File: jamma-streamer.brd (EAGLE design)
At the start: 180.3 x 92 mm, 64 parts, among them IC1 LM7805, J1 Audio line out, J2 ICSP, J4 DM3AT-SF-PEJM5, J5 KMMX-BSMT35S-B30TR, T1 TY-145P, T2 TY-145P, U1 CD74HC165MD16-M, U10 LM358DTD8-M, U2 ATMEGA328PB-AUR, U3 74HC4050D, U4 TLV757X / LP298X, U5 CD74HC165MD16-M, U6 CD74HC165MD16-M, U7 FT232RL, U8 DS3231SNT&R21-0042B_16-M, U9 NDT2955SOT-223-M, Y1 16MHz

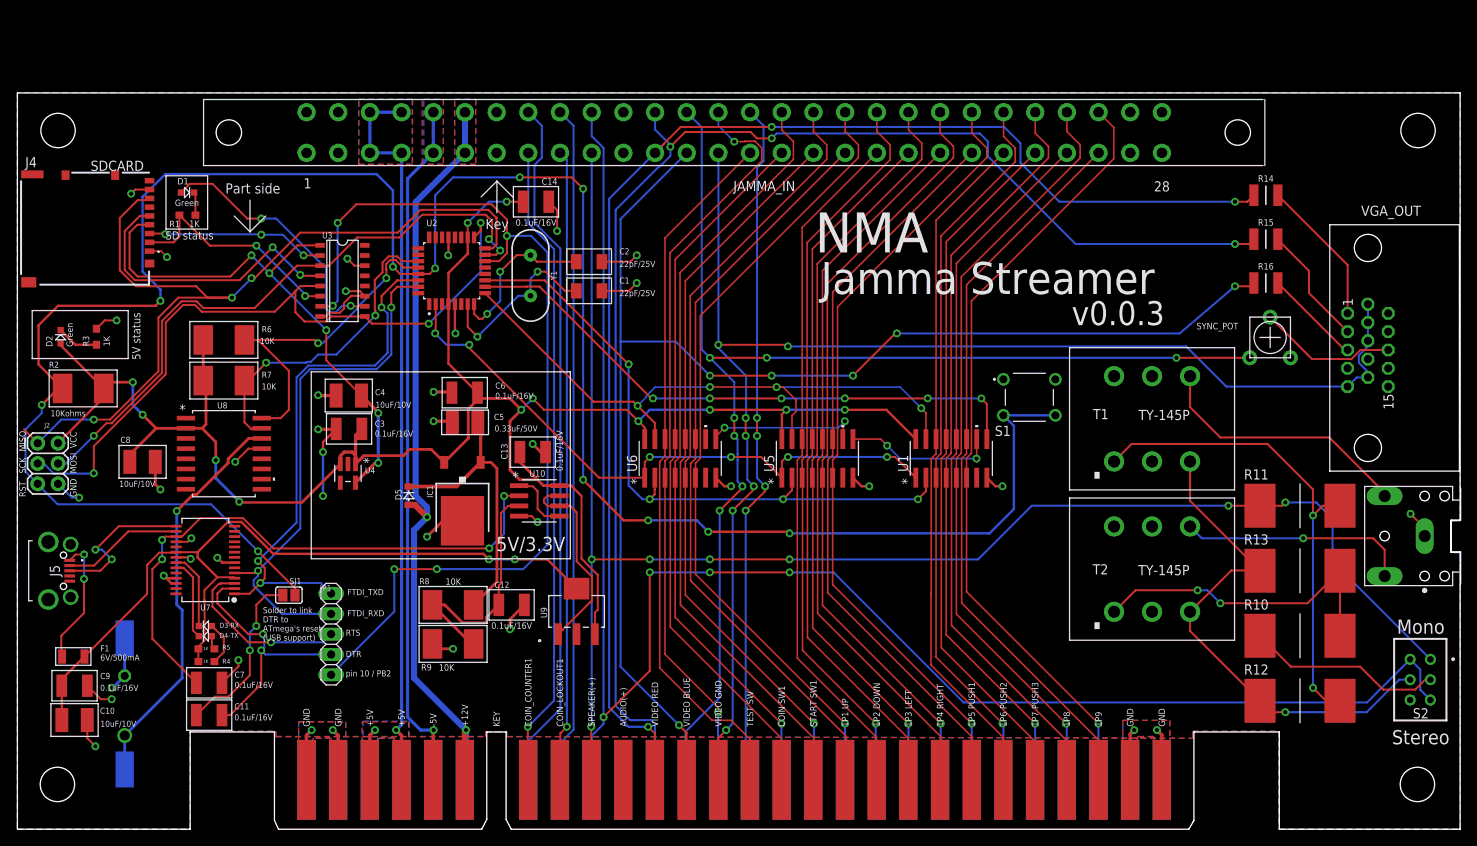
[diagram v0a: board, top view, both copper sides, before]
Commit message: Reorg eagle libraries
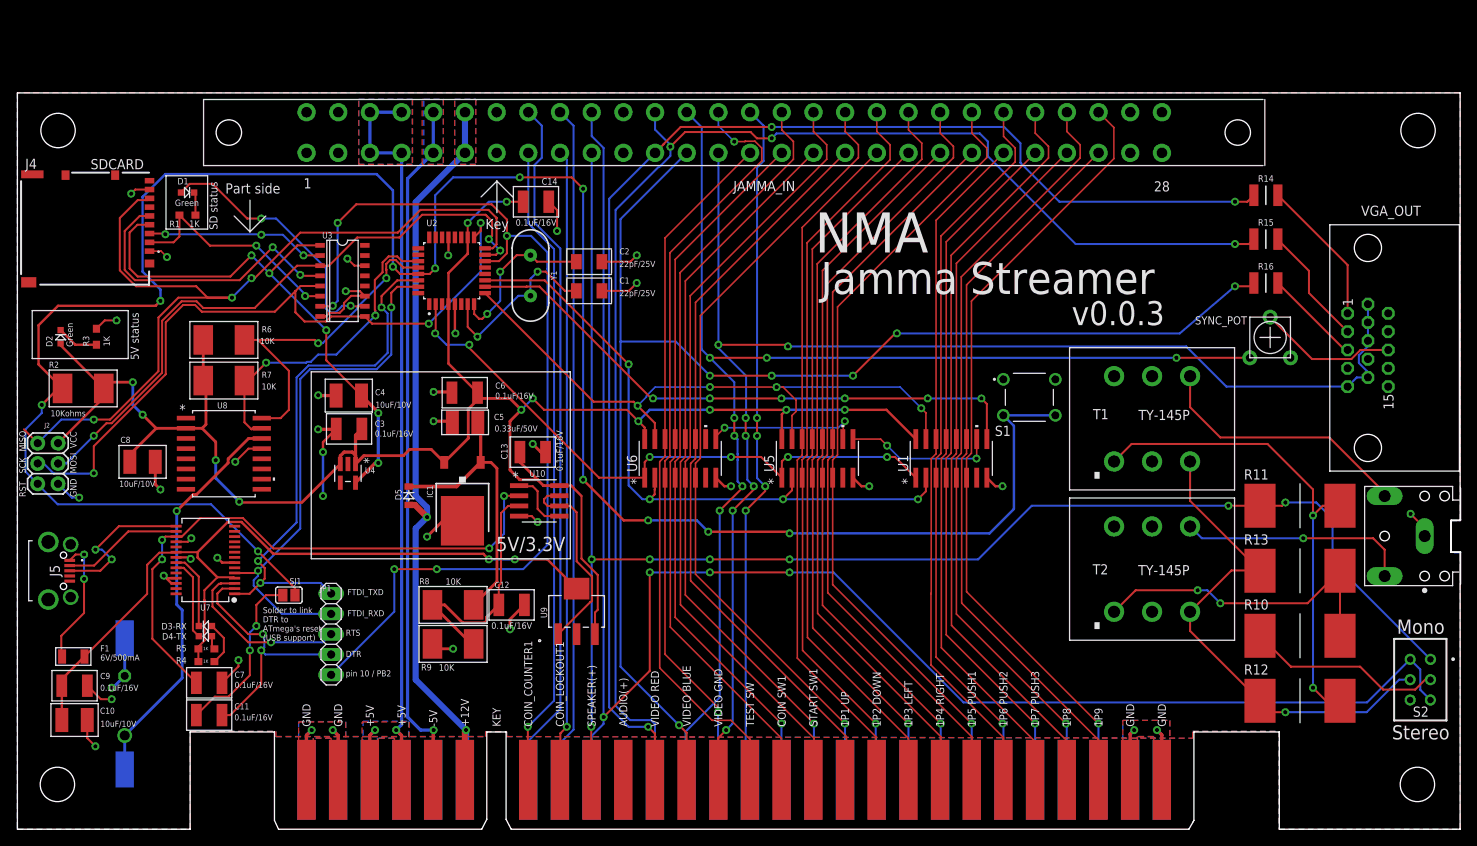
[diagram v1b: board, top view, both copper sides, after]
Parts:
- B1: device S8411R:S8411-45R -> nma-eagle:S8411-45R
- C1, C2: device CMS:KEMET-C1206C334M5RAC -> nma-eagle:KEMET-C1206C334M5RAC
- C10, C4, C8: device CMS:KEMET-C1210C106K8N -> nma-eagle:KEMET-C1210C106K8N
- C11, C12, C13, C14, C3, C6, C7, C9: device CMS:KEMET-C1210C104K4J -> nma-eagle:KEMET-C1210C104K4J
- C5: device CMS:KEMET-C1206X334K5R -> nma-eagle:KEMET-C1206X334K5R
- D1, D2, D3-RX, D4-TX: device CMS:604-APTD1608LCGCK -> nma-eagle:604-APTD1608LCGCK
- D5: device RRE07VTM4SFHTR:DIODE-RRE07VTM4SFHTR -> nma-eagle:DIODE-RRE07VTM4SFHTR
- F1: device 1206L050YR:FUSE-1206L050YR -> nma-eagle:FUSE-1206L050YR
- J1: device SJ1-3523N:CUI_SJ1-3523N -> nma-eagle:CUI_SJ1-3523N
- J4: device DM3AT-SF-PEJM5:DM3AT-SF-PEJM5_1 -> nma-eagle:DM3AT-SF-PEJM5_1
- J5: device KMMX-BSMT35S-B30TR:KMMXBSMT35SB30TR -> nma-eagle:KMMXBSMT35SB30TR
- JAMMA_IN: device jamma_female_56:JAMMA_FEMALE_56 -> nma-eagle:JAMMA_FEMALE_56
- JAMMA_OUT_BTM: device JAMMA:JAMMA_BOTTOM -> nma-eagle:JAMMA_BOTTOM
- JAMMA_OUT_TOP: device JAMMA:JAMMA_TOP -> nma-eagle:JAMMA_TOP
- R1, R3, R4, R5: device CMS:652-CHP0603FX1001ELF -> nma-eagle:652-CHP0603FX1001ELF
- R10, R11, R12, R13: device nma-mouser:TE_3550_SERIES -> nma-eagle:TE_3550_SERIES
- R14, R15, R16: device nma-mouser:RESC3225X70N -> nma-eagle:RESC3225X70N
- R2, R6, R7, R8, R9: device CMS:BOURNS-CRM2512AJW-103ELF -> nma-eagle:BOURNS-CRM2512AJW-103ELF
- S1: device 1825910-7:SW_1825910-7 -> nma-eagle:SW_1825910-7
- S2: device SamacSys_Parts:SS22SDP2(DPDT) -> nma-eagle:SS22SDP2(DPDT)
- SYNC_POT: device SparkFun-Retired:TRIM_POT_PTH -> nma-eagle:TRIM_POT_PTH
- T1, T2: device TRIAD-TY-145P:TRIAD-TY-145P -> nma-eagle:TRIAD-TY-145P
- U1, U5, U6: device CD74HC165M:D16-M -> nma-eagle:D16-M
- U10: device LM358D:D8-M -> nma-eagle:D8-M
- U2: device ATMEGA328PB-AUR:QFP80P900X900X120-32N -> nma-eagle:QFP80P900X900X120-32N
- U3: device 74HC4050D:SO16 -> nma-eagle:SO16
- U4: device LP2981-33DBVR:DBV5-M -> nma-eagle:DBV5-M
- U8: device DS3231:21-0042B_16-M -> nma-eagle:21-0042B_16-M
- U9: device NDT2955:SOT-223-M -> nma-eagle:SOT-223-M
- VGA_OUT: device harting-D-Sub-15:HARTING-DSUB-15-FEMALE -> nma-eagle:HARTING-DSUB-15-FEMALE
- Y1: device SparkFun-Clocks:HC49US -> nma-eagle:HC49US

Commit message: Changing battery holder to use CR2032
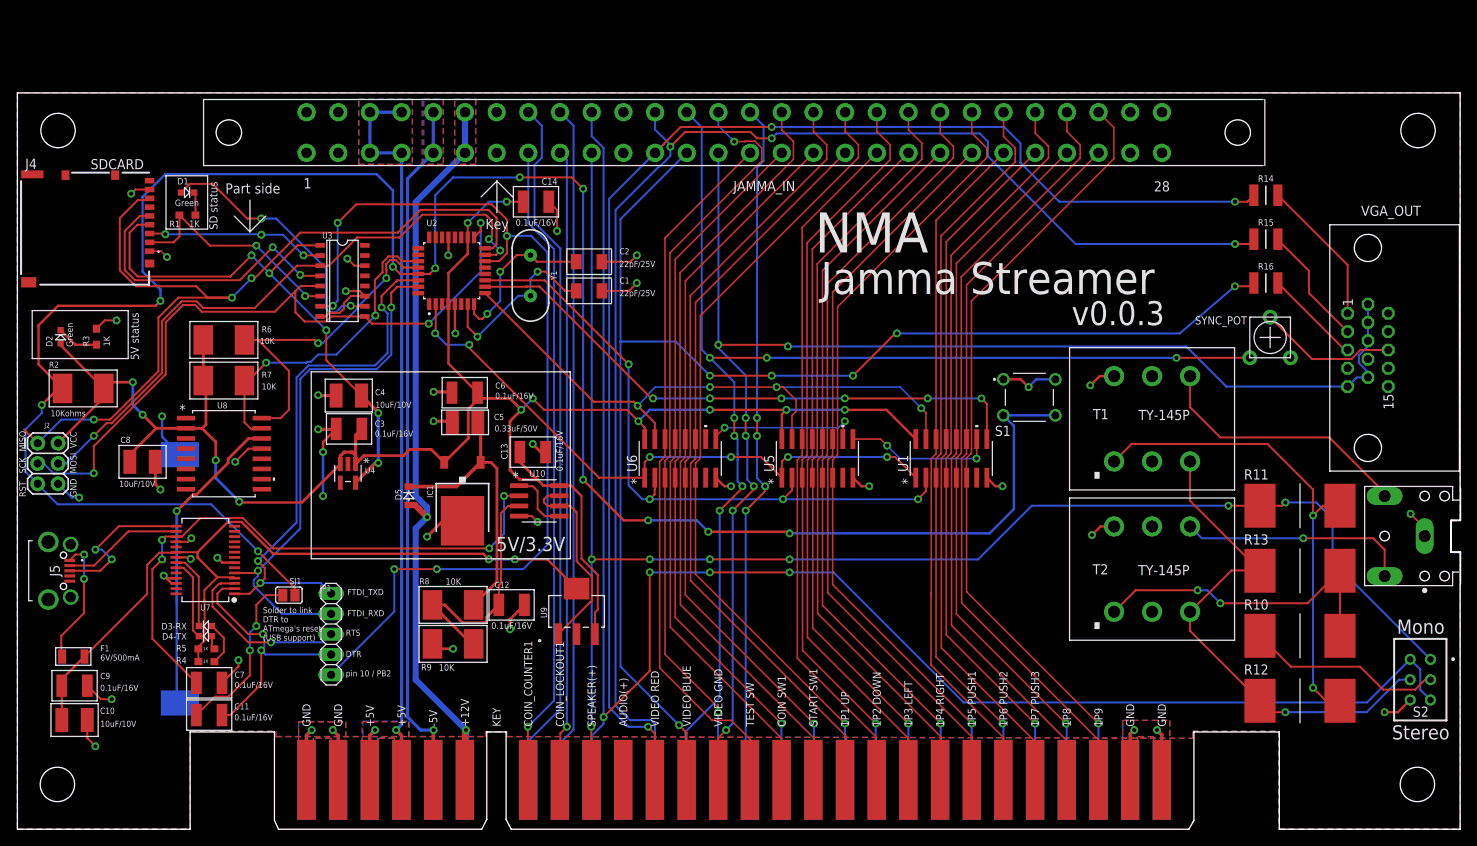
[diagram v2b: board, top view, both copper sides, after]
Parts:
- removed B1: S8411-45R, nma-eagle:S8411-45R
- added J3: 796136-1, nma-eagle:796136-1
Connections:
- net GND: now also J3.2; no longer B1.3, B1.4
- net N$31: now also J3.1; no longer B1.1, B1.2
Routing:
- net GND: track 176.3 -> 192.9 mm, vias 40 -> 44
- net N$31: track 50.2 -> 38.9 mm
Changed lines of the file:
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@@
 <layers>
 <layer number="1" name="Top" color="4" fill="1" visible="yes" active="yes"/>
-<layer number="2" name="Route2" color="16" fill="1" visible="no" active="yes"/>
+<layer number="2" name="Route2" color="16" fill="1" visible="yes" active="yes"/>
 <layer number="3" name="Route3" color="4" fill="3" visible="no" active="no"/>
 <layer number="4" name="Route4" color="1" fill="4" visible="no" active="no"/>
@@
 <layer number="13" name="Route13" color="4" fill="5" visible="no" active="no"/>
 <layer number="14" name="Route14" color="1" fill="6" visible="no" active="no"/>
-<layer number="15" name="Route15" color="23" fill="1" visible="no" active="yes"/>
+<layer number="15" name="Route15" color="23" fill="1" visible="yes" active="yes"/>
 <layer number="16" name="Bottom" color="1" fill="1" visible="yes" active="yes"/>
 <layer number="17" name="Pads" color="2" fill="1" visible="yes" active="yes"/>
@@
 <layer number="25" name="tNames" color="7" fill="1" visible="yes" active="yes"/>
 <layer number="26" name="bNames" color="7" fill="1" visible="yes" active="yes"/>
-<layer number="27" name="tValues" color="7" fill="1" visible="yes" active="yes"/>
+<layer number="27" name="tValues" color="7" fill="1" visible="no" active="yes"/>
 <layer number="28" name="bValues" color="7" fill="1" visible="no" active="yes"/>
 <layer number="29" name="tStop" color="7" fill="3" visible="no" active="yes"/>
@@
 <layer number="44" name="Drills" color="7" fill="1" visible="no" active="yes"/>
 <layer number="45" name="Holes" color="7" fill="1" visible="no" active="yes"/>
-<layer number="46" name="Milling" color="3" fill="1" visible="yes" active="yes"/>
+<layer number="46" name="Milling" color="3" fill="1" visible="no" active="yes"/>
 <layer number="47" name="Measures" color="7" fill="1" visible="no" active="yes"/>
 <layer number="48" name="Document" color="7" fill="1" visible="no" active="yes"/>
@@
 <attribute name="VALUE" x="30.5308" y="54.9656" size="0.762" layer="21"/>
 </element>
-<element name="B1" library="nma-eagle" package="S8411-45R" value="S8411-45R" x="13.4112" y="15.4432" smashed="yes" rot="MR0">
-<attribute name="NAME" x="4.9442" y="16.3732" size="1.27" layer="22" rot="MR0"/>
-</element>
 <element name="C8" library="nma-eagle" package="KEMET-C1210C106K8N" value="10uF/10V" x="15.6464" y="45.9232" smashed="yes">
 <attribute name="NAME" x="12.8728" y="48.2904" size="0.762" layer="21"/>
@@
 <attribute name="NAME" x="156.0576" y="70.3652" size="0.8128" layer="25" align="center"/>
 <attribute name="VALUE" x="156.0576" y="66.1852" size="0.8128" layer="27" align="center"/>
+</element>
+<element name="J3" library="nma-eagle" package="796136-1" value="796136-1" x="20.32" y="31.2928" smashed="yes" rot="MR90">
+<attribute name="DESCRIPTION" value="Holder pcb 2 way Battery TE Connectivity Surface Mount Battery Holder for 1, Leaf Spring Contact" x="20.32" y="31.2928" size="1.778" layer="28" rot="MR90" display="off"/>
+<attribute name="HEIGHT" value="mm" x="20.32" y="31.2928" size="1.778" layer="28" rot="MR90" display="off"/>
+<attribute name="MANUFACTURER_NAME" value="TE Connectivity" x="20.32" y="31.2928" size="1.778" layer="28" rot="MR90" display="off"/>
+<attribute name="MANUFACTURER_PART_NUMBER" value="796136-1" x="20.32" y="31.2928" size="1.778" layer="28" rot="MR90" display="off"/>
+<attribute name="MOUSER_PART_NUMBER" value="571-796136-1" x="20.32" y="31.2928" size="1.778" layer="28" rot="MR90" display="off"/>
+<attribute name="MOUSER_PRICE-STOCK" value="https://www.mouser.co.uk/ProductDetail/TE-Connectivity/796136-1?qs=PfIaAWlFPdz%252BdW7QT0YDTw%3D%3D" x="20.32" y="31.2928" size="1.778" layer="28" rot="MR90" display="off"/>
+<attribute name="NAME" x="31.83636875" y="20.66383125" size="1.27" layer="26" rot="MR90" align="center"/>
+<attribute name="VALUE" x="8.97636875" y="20.66383125" size="1.27" layer="28" rot="MR90" align="center"/>
 </element>
 </elements>
@@
 <via x="37.592" y="49.9872" extent="1-16" drill="0.508"/>
 <wire x1="19.839" y1="30.73" x2="19.8858" y2="30.6832" width="0.254" layer="1"/>
-<contactref element="B1" pad="4"/>
-<contactref element="B1" pad="3"/>
 <contactref element="U8" pad="13"/>
 <wire x1="43.435" y1="70.445" x2="42.1278" y2="70.445" width="0.254" layer="1"/>
@@
 <wire x1="28.8798" y1="47.5742" x2="27.2288" y2="45.9232" width="0.254" layer="1"/>
 <via x="27.2288" y="45.9232" extent="1-16" drill="0.508"/>
-<wire x1="13.4112" y1="23.8682" x2="13.4112" y2="19.1682" width="0.3556" layer="16"/>
-<wire x1="13.4112" y1="19.1682" x2="11.9214" y2="17.6784" width="0.3556" layer="16"/>
-<wire x1="11.9214" y1="17.6784" x2="11.7856" y2="17.6784" width="0.3556" layer="16"/>
-<via x="11.7856" y="17.6784" extent="1-16" drill="0.508"/>
 <contactref element="C8" pad="2"/>
 <wire x1="17.2364" y1="45.9232" x2="17.2364" y2="43.114" width="0.3556" layer="1"/>
@@
 <wire x1="17.9578" y1="72.263" x2="18.6944" y2="71.5264" width="0.2032" layer="1"/>
 <via x="18.6944" y="71.5264" extent="1-16" drill="0.508"/>
+<contactref element="J3" pad="2"/>
+<wire x1="20.32" y1="46.8128" x2="18.0848" y2="49.048" width="0.3048" layer="16"/>
+<wire x1="18.0848" y1="49.048" x2="18.0848" y2="51.6128" width="0.3048" layer="16"/>
+<via x="18.0848" y="51.6128" extent="1-16" drill="0.508"/>
+<wire x1="174.0916" y1="16.1544" x2="172.5676" y2="14.6304" width="0.3048" layer="1"/>
+<wire x1="172.5676" y1="14.6304" x2="170.8912" y2="14.6304" width="0.3048" layer="1"/>
+<via x="170.8912" y="14.6304" extent="1-16" drill="0.508"/>
+<wire x1="137.0838" y1="37.846" x2="135.382" y2="37.846" width="0.3048" layer="1"/>
+<wire x1="135.382" y1="37.846" x2="134.3152" y2="36.7792" width="0.3048" layer="1"/>
+<via x="134.3152" y="36.7792" extent="1-16" drill="0.508"/>
+<wire x1="137.0838" y1="56.63565" x2="135.27405" y2="56.63565" width="0.3048" layer="1"/>
+<wire x1="135.27405" y1="56.63565" x2="134.112" y2="55.4736" width="0.3048" layer="1"/>
+<via x="134.112" y="55.4736" extent="1-16" drill="0.508"/>
+<wire x1="129.74335" y1="56.23855" x2="127.35855" y2="56.23855" width="0.3048" layer="16"/>
+<wire x1="127.35855" y1="56.23855" x2="126.3904" y2="55.2704" width="0.3048" layer="16"/>
+<via x="126.3904" y="55.2704" extent="1-16" drill="0.508"/>
+<wire x1="123.24335" y1="56.23855" x2="125.42225" y2="56.23855" width="0.3048" layer="1"/>
+<wire x1="125.42225" y1="56.23855" x2="126.3904" y2="55.2704" width="0.3048" layer="1"/>
 </signal>
 <signal name="VGROUND">
@@
 <signal name="N$31">
 <contactref element="U8" pad="14"/>
-<contactref element="B1" pad="1"/>
-<contactref element="B1" pad="2"/>
-<wire x1="13.4112" y1="7.4682" x2="13.4112" y2="11.7182" width="0.3556" layer="16"/>
 <via x="19.9136" y="39.7764" extent="1-16" drill="0.508"/>
-<wire x1="19.9136" y1="28.0796375" x2="19.9136" y2="30.6832" width="0.3556" layer="16"/>
-<wire x1="19.9136" y1="39.7764" x2="19.9136" y2="30.6832" width="0.3556" layer="16"/>
-<wire x1="20.5994" y1="27.3938375" x2="19.9136" y2="28.0796375" width="0.3556" layer="16"/>
-<wire x1="20.5994" y1="18.9064" x2="20.5994" y2="27.3938375" width="0.3556" layer="16"/>
-<wire x1="13.4112" y1="11.7182" x2="20.5994" y2="18.9064" width="0.3556" layer="16"/>
+<wire x1="19.9136" y1="39.7764" x2="19.9136" y2="28.0796375" width="0.3556" layer="16"/>
 <wire x1="19.9136" y1="39.7764" x2="21.9583" y2="41.8211" width="0.3556" layer="1"/>
 <wire x1="21.9583" y1="41.8211" x2="22.3701125" y2="41.8211" width="0.3556" layer="1"/>
@@
 <wire x1="26.3398" y1="46.2914375" x2="28.8925625" y2="48.8442" width="0.3556" layer="1"/>
 <wire x1="28.8925625" y1="48.8442" x2="30.5435" y2="48.8442" width="0.3556" layer="1"/>
+<contactref element="J3" pad="1"/>
+<wire x1="19.9136" y1="28.0796375" x2="19.9136" y2="16.1792" width="0.3048" layer="16"/>
+<wire x1="19.9136" y1="16.1792" x2="20.32" y2="15.7728" width="0.3048" layer="16"/>
 </signal>
 <signal name="USBVCC">

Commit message: Added RTC with milliseconds accuracy
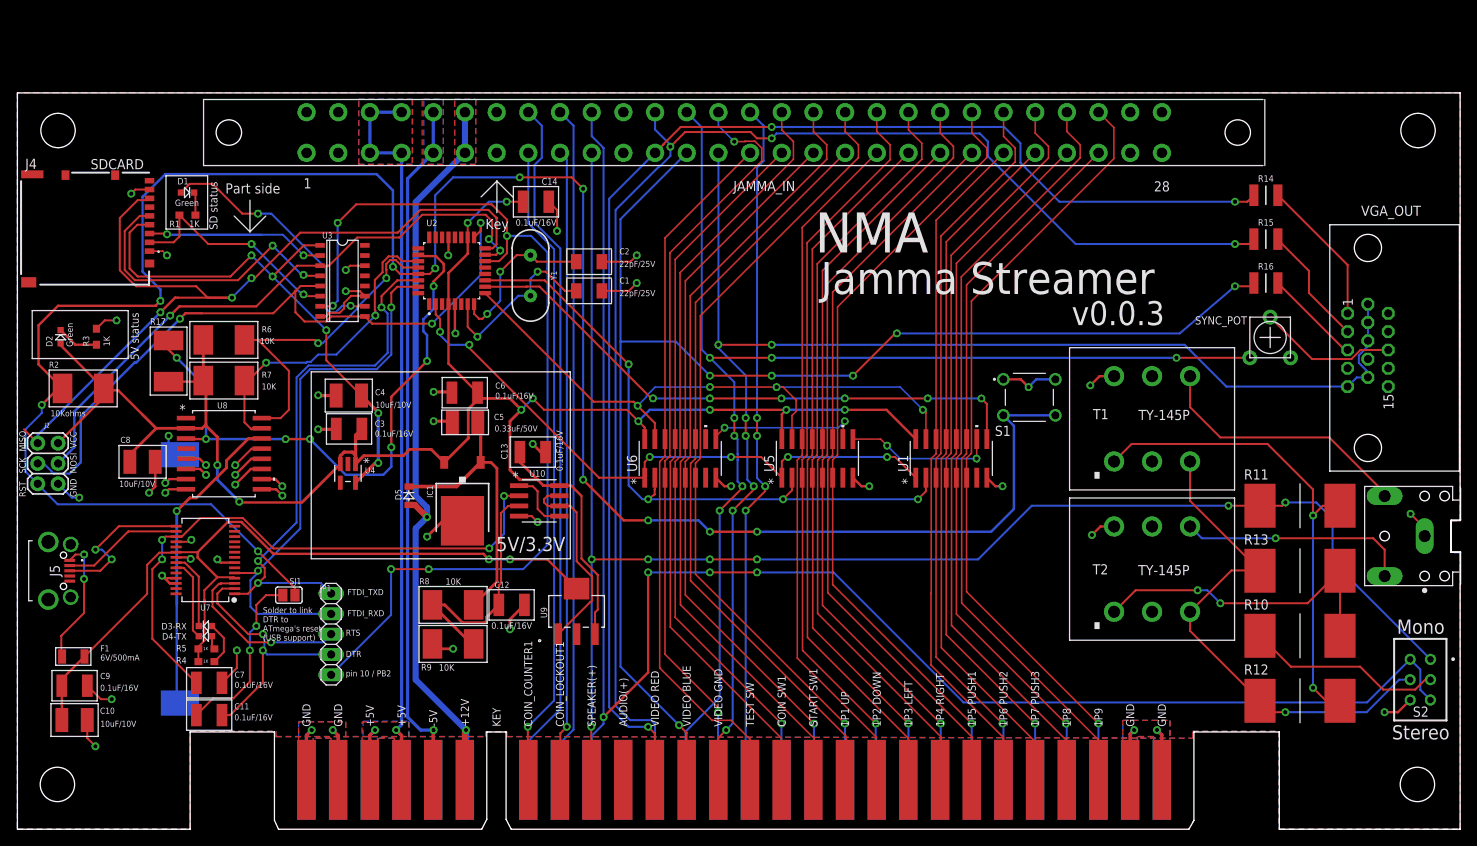
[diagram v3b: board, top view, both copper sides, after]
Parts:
- added R17: 10K, nma-eagle:BOURNS-CRM2512AJW-103ELF
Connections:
- new net RTC_SQW: R17.2, U2.26, U8.3
- net GND: now also U8.10, U8.11, U8.12, U8.5, U8.6, U8.7, U8.8, U8.9
- net VCC: now also R17.1
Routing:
- net RTC_SQW: track 0.00 -> 74.3 mm, vias 0 -> 7
- net GND: track 192.9 -> 208.5 mm, vias 44 -> 50
- net VCC: track 247.0 -> 251.0 mm, vias 12 -> 10
- net DO: track 107.9 -> 104.6 mm
- net CLK: track 89.9 -> 87.0 mm
- net FTDI_RXD: track 66.5 -> 68.6 mm
- net DI: track 78.5 -> 76.6 mm
- net SD_CMD: track 22.9 -> 22.6 mm, vias 3 -> 2
